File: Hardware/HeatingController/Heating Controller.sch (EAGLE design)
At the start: 37 parts, among them IC1 ATMega 328p-pu, IC2 ULN2003AD, K1 G5LE, K2 G5LE, Q1 16MHz, X1 SWITCHED_OUT, X2 MAINS IN, X3 NEUTRAL

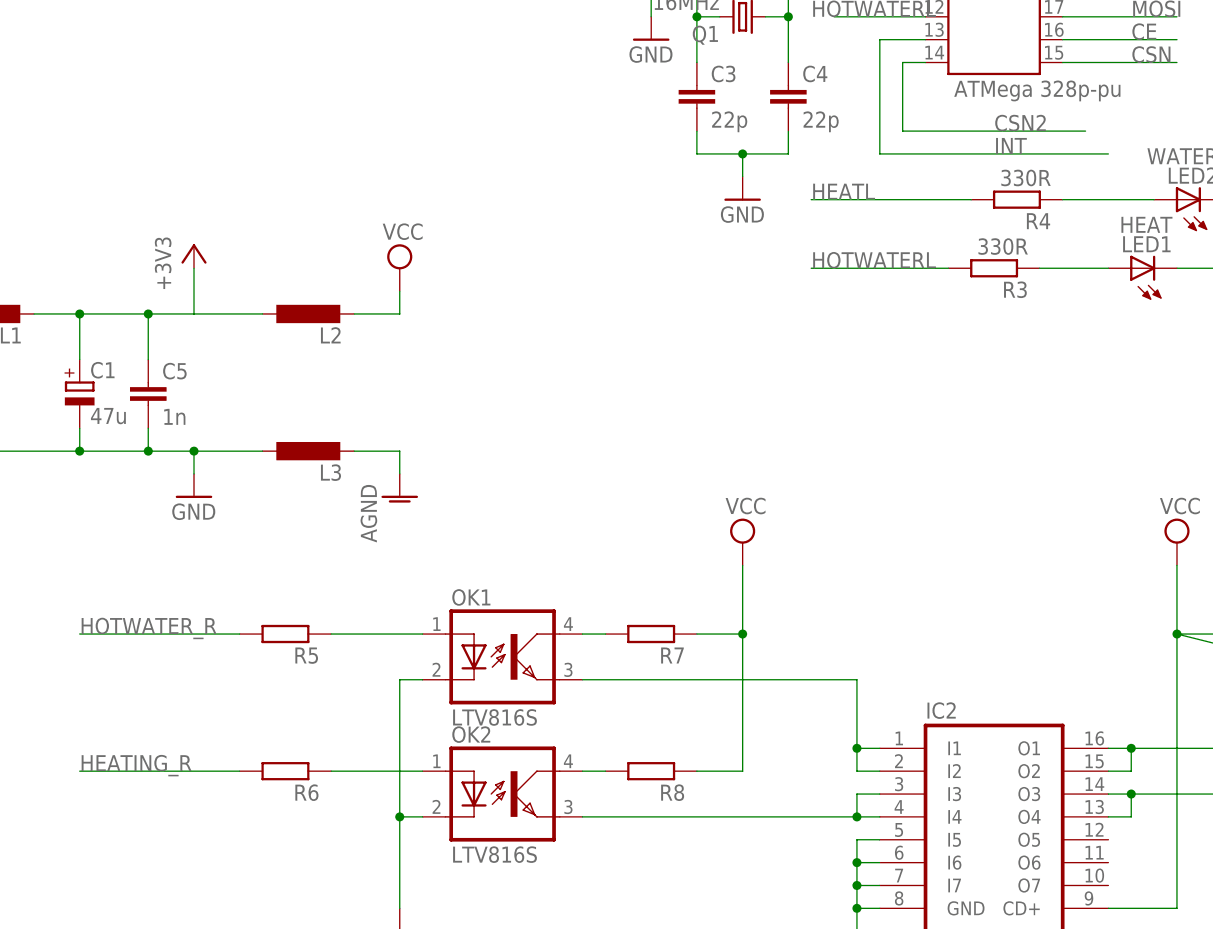
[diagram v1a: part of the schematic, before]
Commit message: updated BOM with finalised pricelist
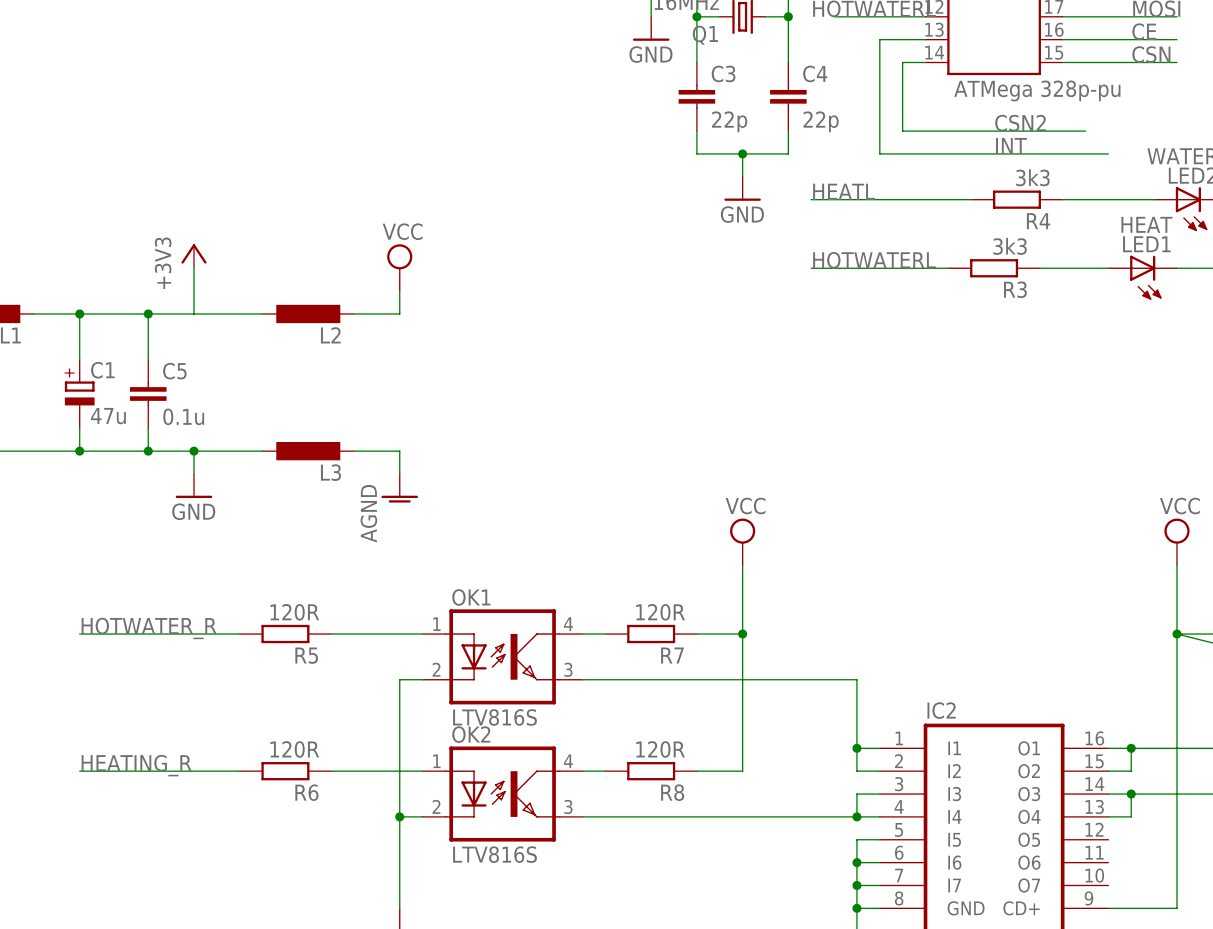
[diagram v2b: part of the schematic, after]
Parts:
- C5: value 1n -> 0.1u
- R3, R4: value 330R -> 3k3
- R5, R6, R7, R8: value (none) -> 120R
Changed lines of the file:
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@@
 <part name="Q1" library="crystal" deviceset="CRYSTAL" device="HC49S" value="16MHz"/>
 <part name="R2" library="rcl" deviceset="R-EU_" device="R1206" value="10k"/>
-<part name="R3" library="rcl" deviceset="R-EU_" device="R1206" value="330R"/>
-<part name="R4" library="rcl" deviceset="R-EU_" device="R1206" value="330R"/>
+<part name="R3" library="rcl" deviceset="R-EU_" device="R1206" value="3k3"/>
+<part name="R4" library="rcl" deviceset="R-EU_" device="R1206" value="3k3"/>
 <part name="C3" library="rcl" deviceset="C-EU" device="C1206K" value="22p"/>
 <part name="C4" library="rcl" deviceset="C-EU" device="C1206K" value="22p"/>
-<part name="C5" library="rcl" deviceset="C-EU" device="C1206K" value="1n"/>
+<part name="C5" library="rcl" deviceset="C-EU" device="C1206K" value="0.1u"/>
 <part name="+3V2" library="supply1" deviceset="+3V3" device=""/>
 <part name="GND2" library="supply1" deviceset="GND" device=""/>
@@
 <part name="SUPPLY1" library="supply2" deviceset="VCC" device=""/>
 <part name="SUPPLY3" library="supply2" deviceset="VCC" device=""/>
-<part name="R5" library="rcl" deviceset="R-EU_" device="R1206"/>
-<part name="R6" library="rcl" deviceset="R-EU_" device="R1206"/>
-<part name="R7" library="rcl" deviceset="R-EU_" device="R1206"/>
-<part name="R8" library="rcl" deviceset="R-EU_" device="R1206"/>
+<part name="R5" library="rcl" deviceset="R-EU_" device="R1206" value="120R"/>
+<part name="R6" library="rcl" deviceset="R-EU_" device="R1206" value="120R"/>
+<part name="R7" library="rcl" deviceset="R-EU_" device="R1206" value="120R"/>
+<part name="R8" library="rcl" deviceset="R-EU_" device="R1206" value="120R"/>
 <part name="L1" library="rcl" deviceset="L-EU" device="L3230M"/>
 <part name="L2" library="rcl" deviceset="L-EU" device="L3230M"/>
